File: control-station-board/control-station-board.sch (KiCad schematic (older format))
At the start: 4 parts

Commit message: Add RS485
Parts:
- added C?: C, symbol Device:C
- added D? (x4): LED, symbol Device:LED
- added J?: USB_B, symbol Connector:USB_B
- added R? (x4): 220, symbol Device:R
- added R? (x2): 10k, symbol Device:R
- added R? (x2): 120, symbol Device:R
- added U?: FT232RL, Package_SO:SSOP-28_5.3x10.2mm_P0.65mm, symbol Interface_USB:FT232RL
- added U?: THVD1550DR, symbol rs485-to-uart:THVD1550DR
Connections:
- net labels added: D, R, RXD, TXD
- wire segments 13 -> 70
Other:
- moved on the sheet: C?, J?, U?

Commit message: Cleaning up schematic
Adding camera decoding
created symbol library
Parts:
- removed C? (x2): C, symbol Device:C
- removed R? (x4): 220, symbol Device:R
- removed R? (x2): 10k, symbol Device:R
- removed R? (x2): 120, symbol Device:R
- added C? (x6): 0.1uF, symbol Device:C
- added R? (x4): 330, symbol Device:R_US
- added R? (x2): 120, symbol Device:R_US
- added R? (x3): 10k, symbol Device:R_US
- added R? (x2): 75, symbol Device:R_US
- added U?: MAX4445, symbol MAX4445:MAX4445
- U?: symbol rs485-to-uart:THVD1550DR -> control-station-board-rescue:THVD1550DR-rs485-to-uart
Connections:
- net labels added: -5V, CAM1+, CAM1-, CAM1_OUT, CANH, CANL, RS485_A, RS485_B
- wire segments 70 -> 108
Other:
- note added: "USB to CAN"
- note added: "USB to RS485"
- moved on the sheet: D?, J?, U?

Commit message: Started component organization on PCB
Added -5V regulator, and other camera decoding circuit
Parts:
- added C3, C4: 10uF, Capacitor_SMD:C_0805_2012Metric, symbol Device:C
- added C5, C7: 0.1uF, Capacitor_SMD:C_0603_1608Metric, symbol Device:C
- added C6: 1uF, Capacitor_SMD:C_0805_2012Metric, symbol Device:C
- added R3, R4: 75, Resistor_SMD:R_0603_1608Metric, symbol Device:R_US
- added U2: LTC1983ES6-5-TRPBF, Package_TO_SOT_SMD:SOT-23-6, symbol LTC1983ES6-5:LTC1983ES6-5-TRPBF
- added U3: MAX4445, Package_SO:SOIC-16_3.9x9.9mm_P1.27mm, symbol MAX4445:MAX4445
- C1, C10, C11, C2, C8, C9: renamed from C?; footprint (none) -> Capacitor_SMD:C_0603_1608Metric
- D1, D2, D3, D4: renamed from D?; footprint (none) -> LED_SMD:LED_0603_1608Metric
- J1, J2: renamed from J?; footprint (none) -> Connector_USB:USB_B_OST_USB-B1HSxx_Horizontal
- R1, R10, R11, R12, R13, R2, R5, R6, R7, R8, R9: renamed from R?; footprint (none) -> Resistor_SMD:R_0603_1608Metric
- U1: renamed from U?; footprint (none) -> Package_SO:SOIC-16_3.9x9.9mm_P1.27mm
- U4, U6: renamed from U?; footprint (none) -> Package_SO:SOIC-8_3.9x4.9mm_P1.27mm
- gave numbers to parts that had none: 2
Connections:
- net +5V: now also C3.1, C5.1, U2.1 (VCC), U2.6 (*SHDN), U3.1 (VCC), U3.2 (VCC), U3.9 (EN)
- net -5V: now also C4.1, C7.1, U2.2 (VOUT), U3.11 (VEE), U3.12 (VEE), U3.13 (VEE), U3.14 (VEE), U3.7 (VEE), U3.8 (VEE)
- net GND: now also C3.2, C4.2, C5.2, C7.2, R4.2, U2.5 (GND), U3.10 (REF), U3.16 (GND)
- new net: R3.1, U3.15 (OUT)
- new net: C6.2, U2.3 (C+)
- new net: C6.1, U2.4 (C-)
- new net CAM2+: U3.6 (IN+)
- new net CAM2-: U3.3 (IN-)
- new net CAM2_OUT: R3.2, R4.1
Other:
- note added: "Camera Decoding for 2 Camera Feeds"
- note added: "Negative Voltage Regulator for Camera Decoding"
- moved on the sheet: C1, C10, C11, C2, C8, C9, D1, D2, D3, D4, J1, J2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

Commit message: Adding full deplex rs485
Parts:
- removed R5, R6: 10k, Resistor_SMD:R_0603_1608Metric, symbol Device:R_US
- removed U4: THVD1550DR, Package_SO:SOIC-8_3.9x4.9mm_P1.27mm, symbol control-station-board-rescue:THVD1550DR-rs485-to-uart
- added F1, F2: 500mA, Fuse:Fuse_0805_2012Metric, symbol Device:Polyfuse
- added J3: CAM1_OUT, RCJ-044:CUI_RCJ-044, symbol Connector:Conn_Coaxial
- added J4: CAM2_OUT, RCJ-044:CUI_RCJ-044, symbol Connector:Conn_Coaxial
- added U?: MAX490E, symbol Interface_UART:MAX490E
- D1, D3: value LED -> TX
- D2, D4: value LED -> RX
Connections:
- net +5V: now also F1.2, F2.2, U?.1 (VCC)
- net CAM1_OUT: now also J3.1 (In)
- net CAM2_OUT: now also J4.1 (In)
- net D: now also U?.3 (DI)
- net GND: now also J3.2 (Ext), J4.2 (Ext), U?.4 (GND)
- net R: now also U?.2 (RO)
- net at J2.1 (VBUS): now also F2.1
- net at J1.1 (VBUS): now also F1.1
- net RS485_A renamed RX_L
- net RX_L: now also U?.7 (B)
- net RS485_B renamed RX_H
- net RX_H: now also U?.8 (A)
- new net TX_H: U?.6 (Z)
- new net TX_L: U?.5 (Y)
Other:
- note added: "Camera Output Connectors"
- note added: "Differential to NTSC for 2 Camera Feeds"
- note removed: "Camera Decoding for 2 Camera Feeds"
- moved on the sheet: C1, C10, C11, C2, C3, C4, C5, C6, C7, C8, C9, D1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

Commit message: working on pcb layout
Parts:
- added J?: Tether Interface, symbol Connector_Generic:Conn_02x06_Counter_Clockwise
- added J?: USB D+/D-, symbol Connector:Conn_01x02_Male
- J1, J2: footprint Connector_USB:USB_B_OST_USB-B1HSxx_Horizontal -> Connector_USB:USB_B_TE_5787834_Vertical
- U4: renamed from U?; footprint (none) -> Package_SO:SOIC-8_3.9x4.9mm_P1.27mm
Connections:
- net CAM1_OUT: now also J?.1 (Pin_1)
- net CAM2_OUT: now also J?.2 (Pin_2)
- net CANH: now also J?.3 (Pin_3)
- net CANL: now also J?.4 (Pin_4)
- net RX_H: now also J?.12 (Pin_12)
- net RX_L: now also J?.11 (Pin_11)
- net TX_H: now also U4.5 (Y), J?.10 (Pin_10); no longer U4.6 (Z)
- net TX_L: now also U4.6 (Z), J?.9 (Pin_9); no longer U4.5 (Y)
- new net: J?.1 (Pin_1), J?.5 (Pin_5)
- new net: J?.2 (Pin_2), J?.6 (Pin_6)
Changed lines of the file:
@@
 F 0 "J2" H 5321 2041 50  0000 R CNN
 F 1 "USB_B" H 5321 1950 50  0000 R CNN
-F 2 "Connector_USB:USB_B_OST_USB-B1HSxx_Horizontal" H 5700 2000 50  0001 C CNN
+F 2 "Connector_USB:USB_B_TE_5787834_Vertical" H 5700 2000 50  0001 C CNN
 F 3 " ~" H 5700 2000 50  0001 C CNN
 	1    5550 2050
@@
 F 0 "J1" H 1221 2041 50  0000 R CNN
 F 1 "USB_B" H 1221 1950 50  0000 R CNN
-F 2 "Connector_USB:USB_B_OST_USB-B1HSxx_Horizontal" H 1600 2000 50  0001 C CNN
+F 2 "Connector_USB:USB_B_TE_5787834_Vertical" H 1600 2000 50  0001 C CNN
 F 3 " ~" H 1600 2000 50  0001 C CNN
 	1    1450 2050
@@
 	5850 1800 5850 1850
 $Comp
-L Interface_UART:MAX490E U?
+L Interface_UART:MAX490E U4
 U 1 1 5BE957F5
 P 2550 4550
-F 0 "U?" H 2650 5100 50  0000 C CNN
+F 0 "U4" H 2650 5100 50  0000 C CNN
 F 1 "MAX490E" H 2750 5000 50  0000 C CNN
-F 2 "" H 2550 3950 50  0001 C CNN
+F 2 "Package_SO:SOIC-8_3.9x4.9mm_P1.27mm" H 2550 3950 50  0001 C CNN
 F 3 "https://datasheets.maximintegrated.com/en/ds/MAX1487E-MAX491E.pdf" H 2310 5000 50  0001 C CNN
 	1    2550 4550
@@
 	2950 4750 2950 4950
 Text GLabel 3350 4650 2    50   Input ~ 0
+TX_L
+Text GLabel 3350 4950 2    50   Input ~ 0
 TX_H
-Text GLabel 3350 4950 2    50   Input ~ 0
-TX_L
 Wire Wire Line
 	3150 4150 3350 4150
@@
 Wire Wire Line
 	2950 4950 3350 4950
+$Comp
+L Connector_Generic:Conn_02x06_Counter_Clockwise J?
+U 1 1 5BF1F400
+P 6450 7100
+F 0 "J?" H 6500 7517 50  0000 C CNN
+F 1 "Tether Interface" H 6500 7426 50  0000 C CNN
+F 2 "" H 6450 7100 50  0001 C CNN
+F 3 "~" H 6450 7100 50  0001 C CNN
+	1    6450 7100
+	1    0    0    -1
+$EndComp
+Text GLabel 6850 6900 2    50   Input ~ 0
+RX_H
+Text GLabel 6850 7000 2    50   Input ~ 0
+RX_L
+Text GLabel 6850 7100 2    50   Input ~ 0
+TX_H
+Text GLabel 6850 7200 2    50   Input ~ 0
+TX_L
+Text GLabel 6150 7100 0    50   Input ~ 0
+CANH
+Text GLabel 6150 7200 0    50   Input ~ 0
+CANL
+Text GLabel 6150 7000 0    50   Input ~ 0
+CAM2_OUT
+Text GLabel 6150 6900 0    50   Input ~ 0
+CAM1_OUT
+Wire Wire Line
+	6750 6900 6850 6900
+Wire Wire Line
+	6750 7000 6850 7000
+Wire Wire Line
+	6750 7100 6850 7100
+Wire Wire Line
+	6750 7200 6850 7200
+Wire Wire Line
+	6250 6900 6150 6900
+Wire Wire Line
+	6250 7000 6150 7000
+Wire Wire Line
+	6250 7100 6150 7100
+Wire Wire Line
+	6250 7200 6150 7200
+$Comp
+L Connector:Conn_01x02_Male J?
+U 1 1 5BF81CF9
+P 6050 7700
+F 0 "J?" V 6203 7513 50  0000 R CNN
+F 1 "USB D+/D-" V 6112 7513 50  0000 R CNN
+F 2 "" H 6050 7700 50  0001 C CNN
+F 3 "~" H 6050 7700 50  0001 C CNN
+	1    6050 7700
+	0    -1   -1   0
+$EndComp
+Wire Wire Line
+	6250 7400 6150 7400
+Wire Wire Line
+	6150 7400 6150 7500
+Wire Wire Line
+	6250 7300 6050 7300
+Wire Wire Line
+	6050 7300 6050 7500
 $EndSCHEMATC

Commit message: Finishing pcb routing
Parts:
- removed J?: Tether Interface, symbol Connector_Generic:Conn_02x06_Counter_Clockwise
- added J6: Conn_02x06_Odd_Even, Connector_PinHeader_2.54mm:PinHeader_2x06_P2.54mm_Vertical, symbol Connector_Generic:Conn_02x06_Odd_Even
- J5: renamed from J?; footprint (none) -> Connector_PinHeader_2.54mm:PinHeader_1x02_P2.54mm_Vertical
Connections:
- net CAM1+: now also J6.7 (Pin_7)
- net CAM1-: now also J6.5 (Pin_5)
- net CAM2+: now also J6.3 (Pin_3)
- net CAM2-: now also J6.1 (Pin_1)
- net CANH: now also J6.4 (Pin_4)
- net CANL: now also J6.2 (Pin_2)
- net D: now also U5.1 (TXD); no longer U5.5 (RXD)
- net R: now also U5.5 (RXD); no longer U5.1 (TXD)
- net RXD: now also U7.5 (RXD); no longer U7.1 (TXD)
- net RX_H: now also J6.12 (Pin_12)
- net RX_L: now also J6.10 (Pin_10)
- net TXD: now also U7.1 (TXD); no longer U7.5 (RXD)
- net TX_H: now also J6.6 (Pin_6)
- net TX_L: now also J6.8 (Pin_8)
- net at J5.1 (Pin_1): now also J6.9 (Pin_9)
- net at J5.2 (Pin_2): now also J6.11 (Pin_11)
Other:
- note added: "Tether Interface"
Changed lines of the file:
@@
 	0    -1   -1   0
 $EndComp
-Text GLabel 3550 1850 2    50   Input ~ 0
+Text GLabel 3550 1750 2    50   Input ~ 0
 D
 Text GLabel 2050 4650 0    50   Input ~ 0
@@
 Text GLabel 2050 4450 0    50   Input ~ 0
 R
-Text GLabel 3550 1750 2    50   Input ~ 0
+Text GLabel 3550 1850 2    50   Input ~ 0
 R
 $Comp
@@
 Text GLabel 6350 4300 0    50   Input ~ 0
 TXD
-Text GLabel 7800 1850 2    50   Input ~ 0
+Text GLabel 7800 1750 2    50   Input ~ 0
 TXD
 Text GLabel 6350 4900 0    50   Input ~ 0
 RXD
-Text GLabel 7800 1750 2    50   Input ~ 0
+Text GLabel 7800 1850 2    50   Input ~ 0
 RXD
 Wire Wire Line
@@
 Wire Wire Line
 	2950 4950 3350 4950
-$Comp
-L Connector_Generic:Conn_02x06_Counter_Clockwise J?
-U 1 1 5BF1F400
-P 6450 7100
-F 0 "J?" H 6500 7517 50  0000 C CNN
-F 1 "Tether Interface" H 6500 7426 50  0000 C CNN
-F 2 "" H 6450 7100 50  0001 C CNN
-F 3 "~" H 6450 7100 50  0001 C CNN
-	1    6450 7100
-	1    0    0    -1
-$EndComp
-Text GLabel 6850 6900 2    50   Input ~ 0
+Text GLabel 6850 7400 2    50   Input ~ 0
 RX_H
-Text GLabel 6850 7000 2    50   Input ~ 0
+Text GLabel 6850 7300 2    50   Input ~ 0
 RX_L
 Text GLabel 6850 7100 2    50   Input ~ 0
@@
 Text GLabel 6850 7200 2    50   Input ~ 0
 TX_L
-Text GLabel 6150 7100 0    50   Input ~ 0
+Text GLabel 6850 7000 2    50   Input ~ 0
 CANH
-Text GLabel 6150 7200 0    50   Input ~ 0
+Text GLabel 6850 6900 2    50   Input ~ 0
 CANL
-Text GLabel 6150 7000 0    50   Input ~ 0
-CAM2_OUT
-Text GLabel 6150 6900 0    50   Input ~ 0
-CAM1_OUT
 Wire Wire Line
 	6750 6900 6850 6900
@@
 	6250 7200 6150 7200
 $Comp
-L Connector:Conn_01x02_Male J?
+L Connector:Conn_01x02_Male J5
 U 1 1 5BF81CF9
 P 6050 7700
-F 0 "J?" V 6203 7513 50  0000 R CNN
+F 0 "J5" V 6203 7513 50  0000 R CNN
 F 1 "USB D+/D-" V 6112 7513 50  0000 R CNN
-F 2 "" H 6050 7700 50  0001 C CNN
+F 2 "Connector_PinHeader_2.54mm:PinHeader_1x02_P2.54mm_Vertical" H 6050 7700 50  0001 C CNN
 F 3 "~" H 6050 7700 50  0001 C CNN
 	1    6050 7700
@@
 Wire Wire Line
 	6050 7300 6050 7500
+Text Notes 5900 6700 0    100  ~ 0
+Tether Interface
+Text GLabel 6150 7000 0    50   Input ~ 0
+CAM2+
+Text GLabel 6150 6900 0    50   Input ~ 0
+CAM2-
+Text GLabel 6150 7200 0    50   Input ~ 0
+CAM1+
+Text GLabel 6150 7100 0    50   Input ~ 0
+CAM1-
+$Comp
+L Connector_Generic:Conn_02x06_Odd_Even J6
+U 1 1 5BE19CB5
+P 6450 7100
+F 0 "J6" H 6500 7425 50  0000 C CNN
+F 1 "Conn_02x06_Odd_Even" H 6500 7426 50  0001 C CNN
+F 2 "Connector_PinHeader_2.54mm:PinHeader_2x06_P2.54mm_Vertical" H 6450 7100 50  0001 C CNN
+F 3 "~" H 6450 7100 50  0001 C CNN
+	1    6450 7100
+	1    0    0    -1
+$EndComp
+Wire Wire Line
+	6750 7300 6850 7300
+Wire Wire Line
+	6750 7400 6850 7400
+Wire Notes Line
+	5750 6500 7200 6500
+Wire Notes Line
+	7200 6500 7200 7800
+Wire Notes Line
+	7200 7800 5750 7800
+Wire Notes Line
+	5750 7800 5750 6500
 $EndSCHEMATC

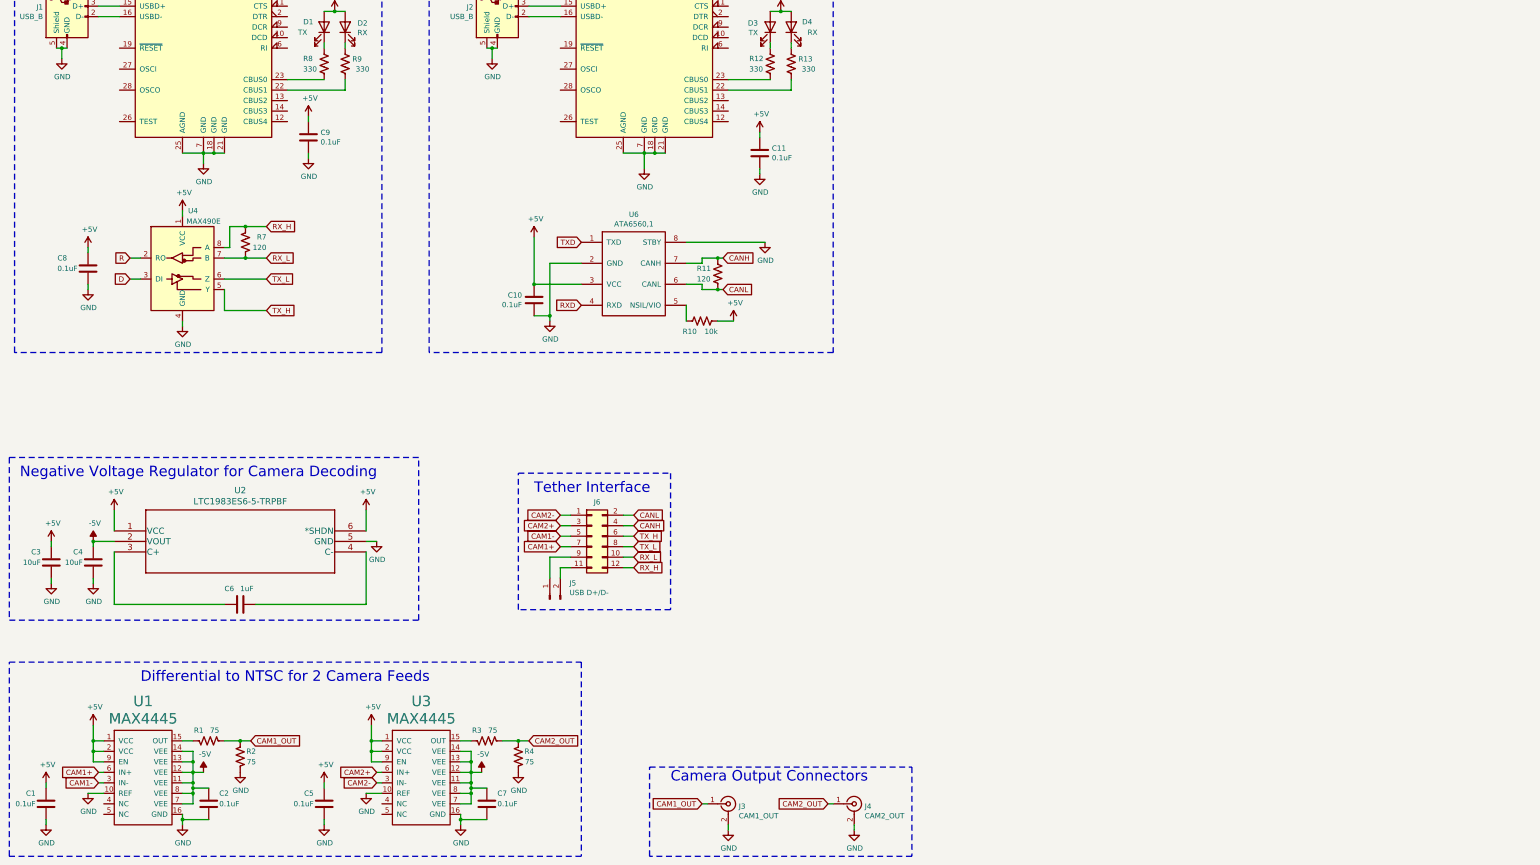
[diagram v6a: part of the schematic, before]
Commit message: Finished PCB routing and silkscreen
Created 3d model,
Created gerber files
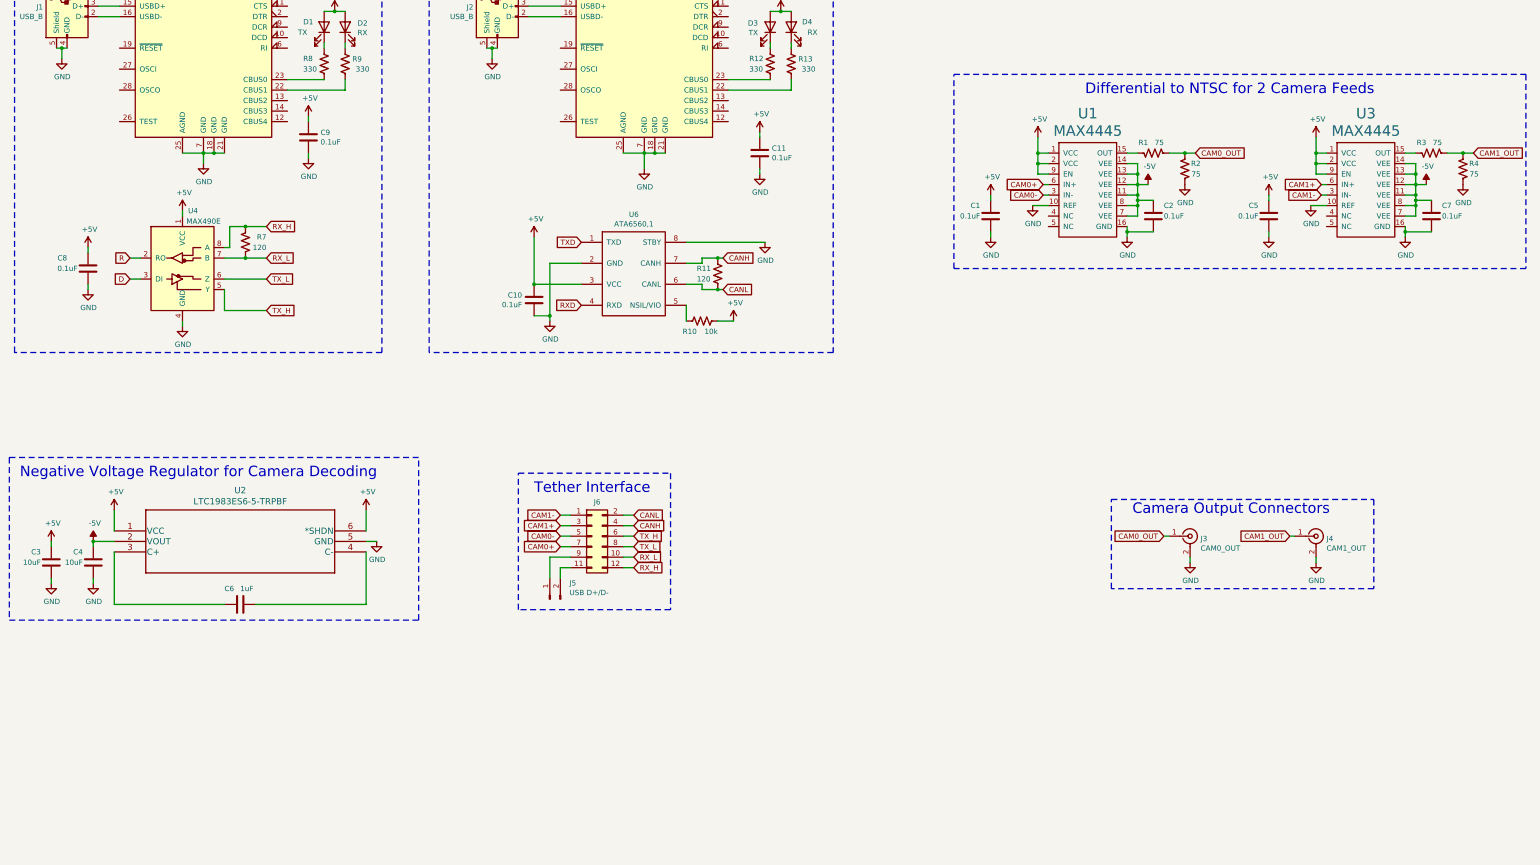
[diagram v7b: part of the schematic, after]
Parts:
- J3: value CAM1_OUT -> CAM0_OUT
- J4: value CAM2_OUT -> CAM1_OUT
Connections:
- net CAM2+ is gone; now on net CAM1+: J6.3 (Pin_3), U3.6 (IN+)
- net CAM2- is gone; now on net CAM1-: J6.1 (Pin_1), U3.3 (IN-)
- net CAM2_OUT is gone; now on net CAM1_OUT: J4.1 (In), R3.2, R4.1
- net CAM1+: no longer J6.7 (Pin_7), U1.6 (IN+)
- net CAM1-: no longer J6.5 (Pin_5), U1.3 (IN-)
- net CAM1_OUT: no longer J3.1 (In), R1.2, R2.1
- new net CAM0+: J6.7 (Pin_7), U1.6 (IN+)
- new net CAM0-: J6.5 (Pin_5), U1.3 (IN-)
- new net CAM0_OUT: J3.1 (In), R1.2, R2.1
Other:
- moved on the sheet: C1, C2, C5, C7, J3, J4, R1, R2, R3, R4, U1, U3
